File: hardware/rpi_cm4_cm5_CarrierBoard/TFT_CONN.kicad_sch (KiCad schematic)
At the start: 22 parts, among them J8 62684-402100ALF, J9 5051101092

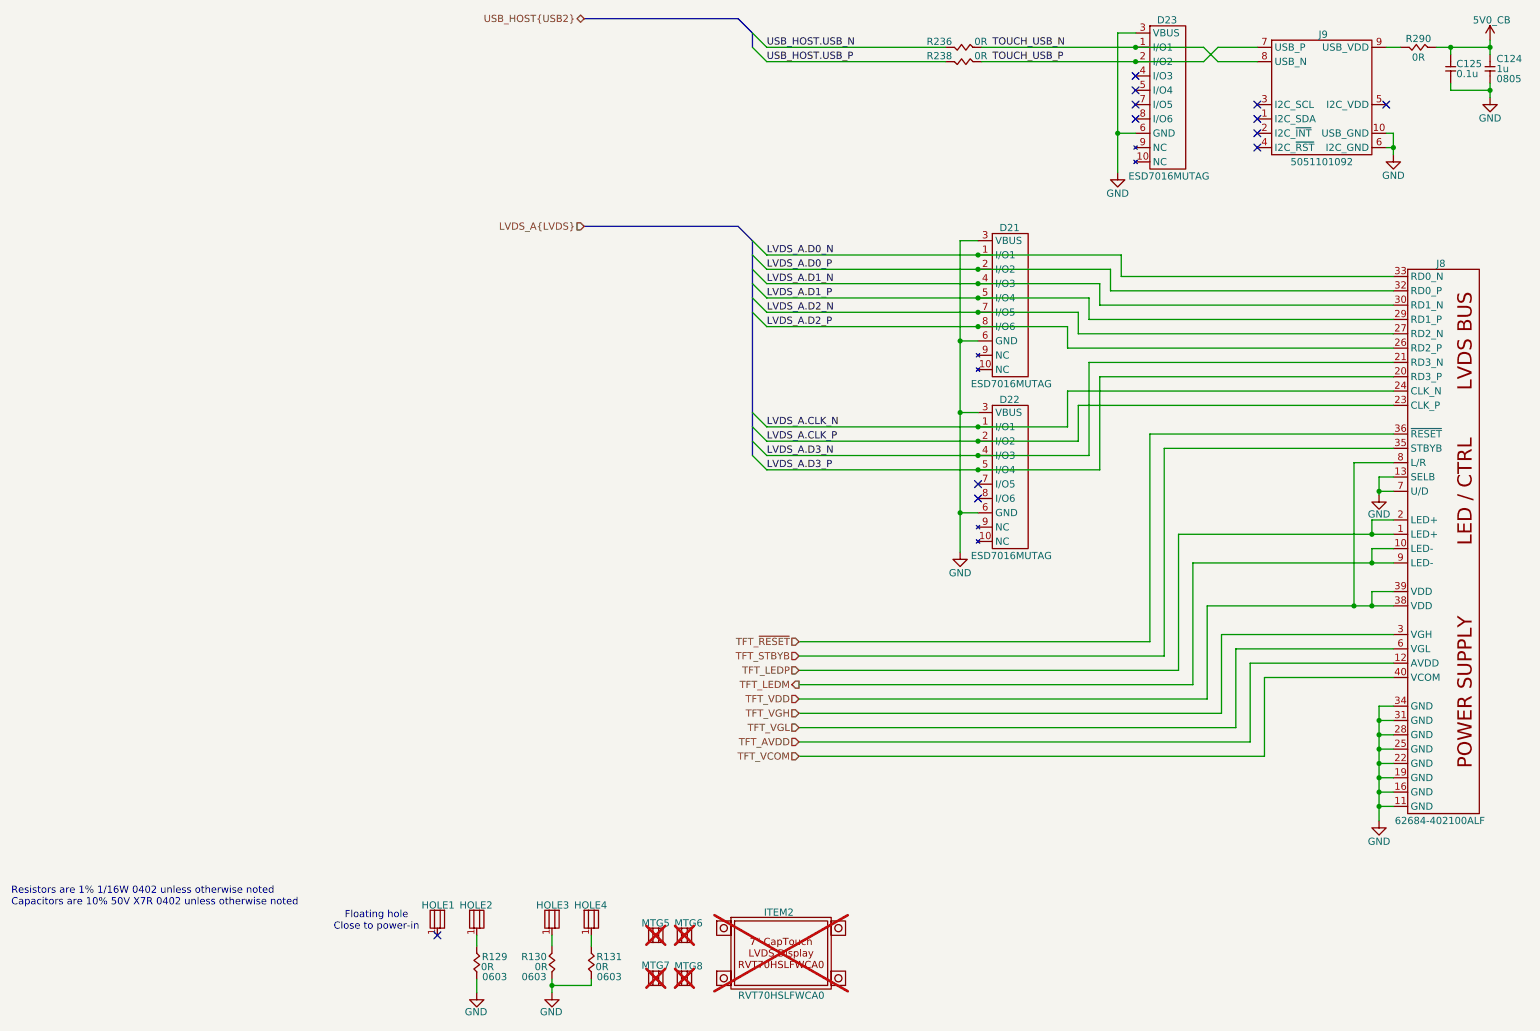
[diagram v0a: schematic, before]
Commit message: Final commit prior to formal DFM by PCB manufacturer & PCBA Several iterations of DRC checks and validation with CAM software completed Ready for quotation
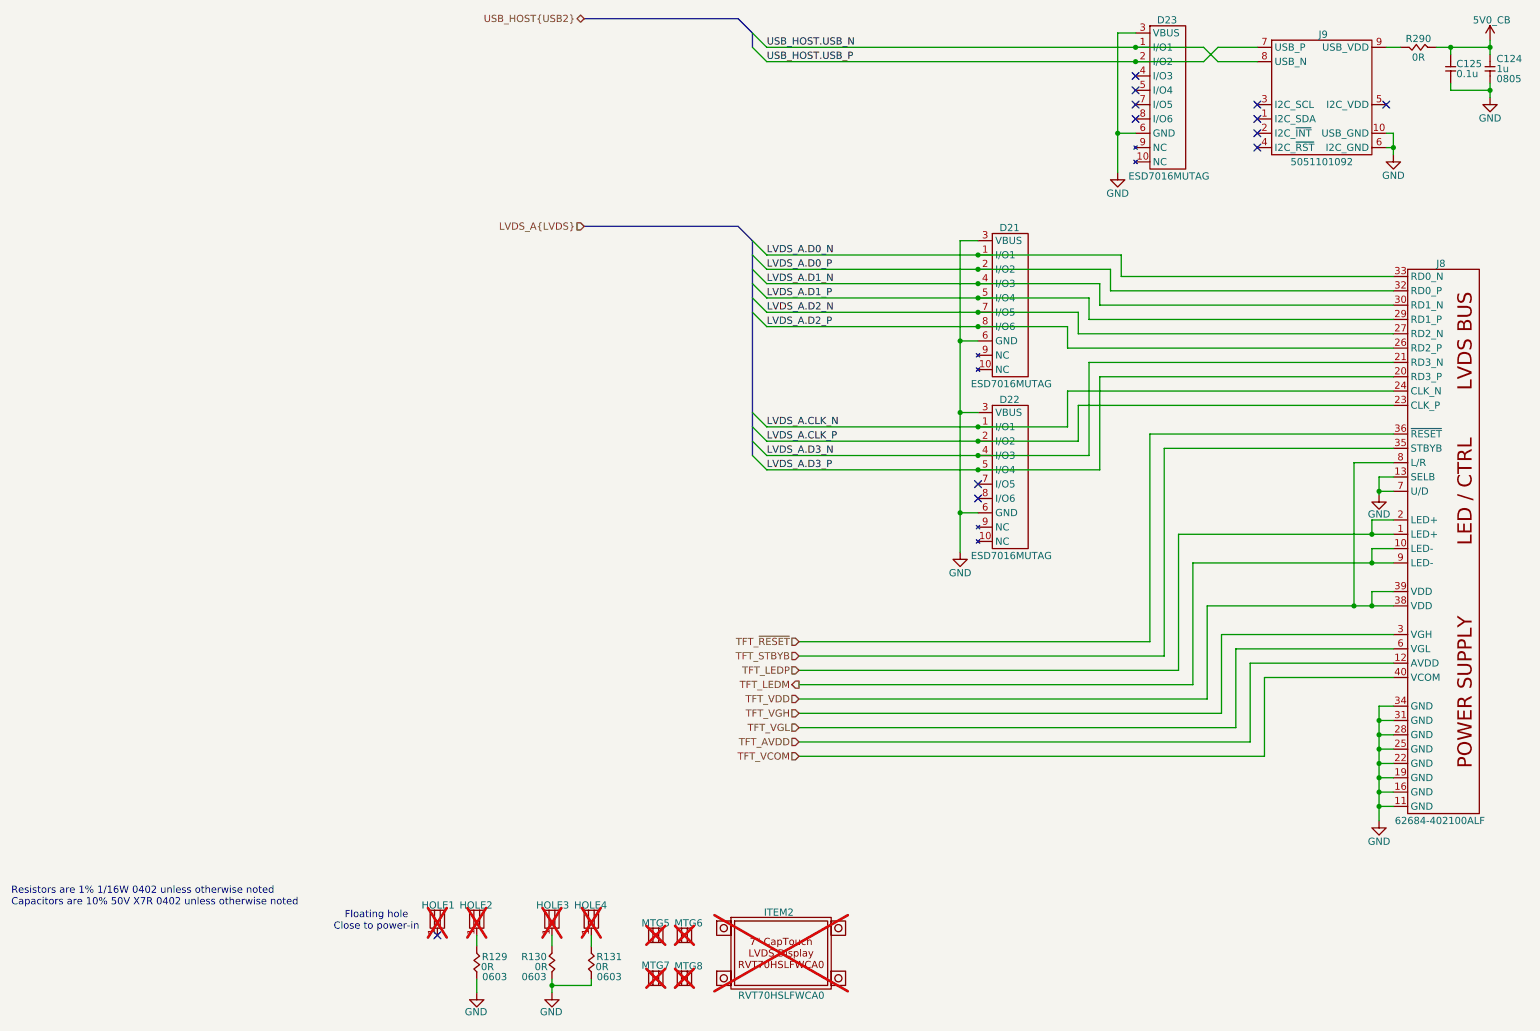
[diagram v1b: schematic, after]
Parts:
- removed R236, R238: 0R, footprint:RES_0402, symbol KicadCompDb:Resistors/RES_SMT_00001
- HOLE1, HOLE2, HOLE3, HOLE4: now not fitted; now left out of the parts list
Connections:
- net TOUCH_USB_N is gone; now on net USB_HOST.USB_N: D23.1 (I/O1), J9.8 (USB_N)
- net TOUCH_USB_P is gone; now on net USB_HOST.USB_P: D23.2 (I/O2), J9.7 (USB_P)
